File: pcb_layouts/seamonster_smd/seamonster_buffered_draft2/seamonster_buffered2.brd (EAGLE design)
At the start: 172.5 x 106.5 mm, 132 parts, among them IC1 7808DT, IC2 4051D, IC3 4051D, IC4 DG408DY, IC5 4046D, IC6 40106D, IC7 4070D, IC8 4046D, IC9 4040D, Q1 THONKICONNNEW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

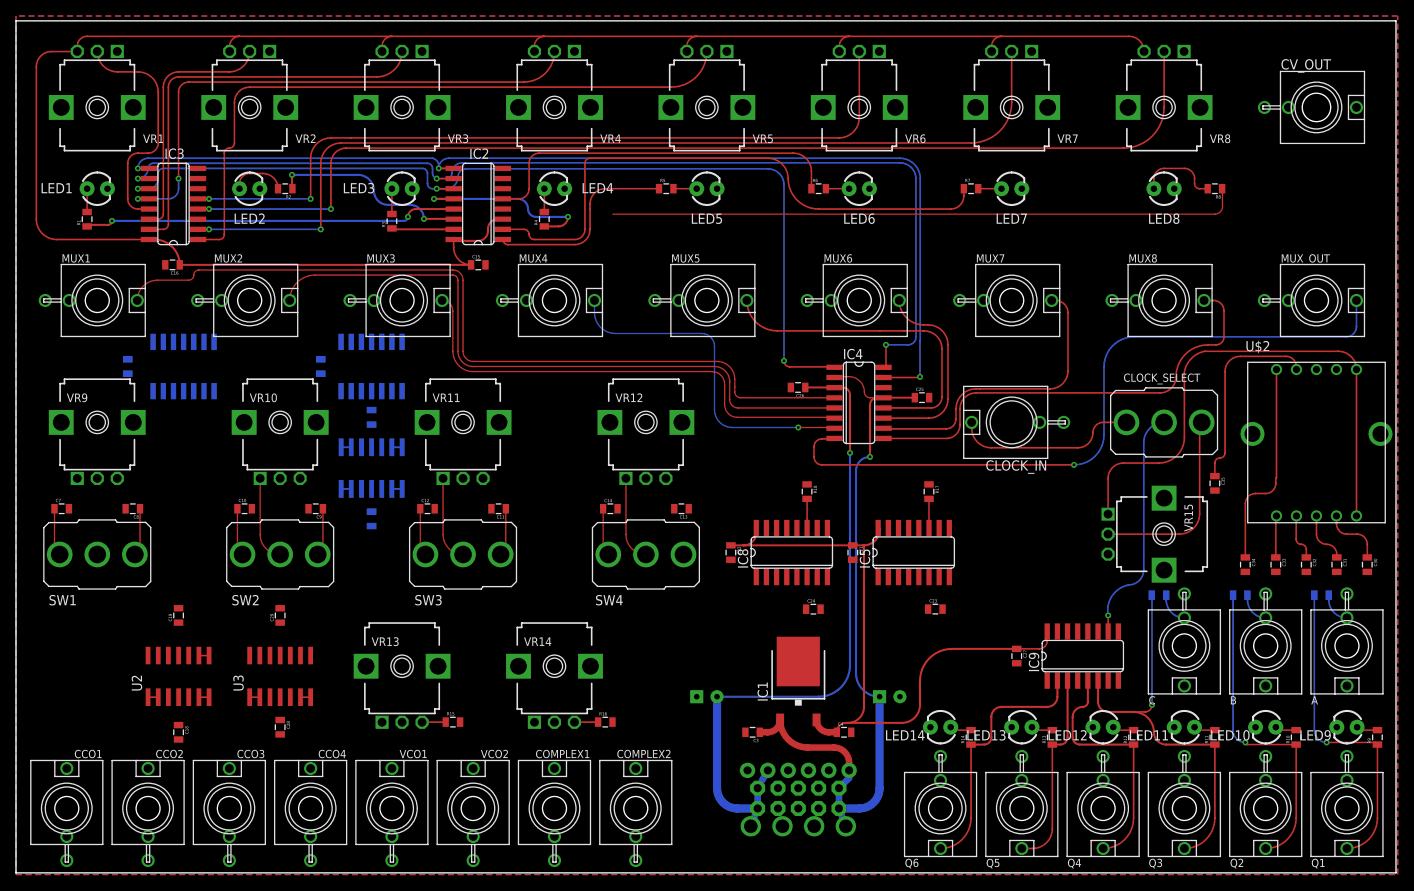
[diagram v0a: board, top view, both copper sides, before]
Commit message: finished routing ABC bus to jacks, began routing oscillators
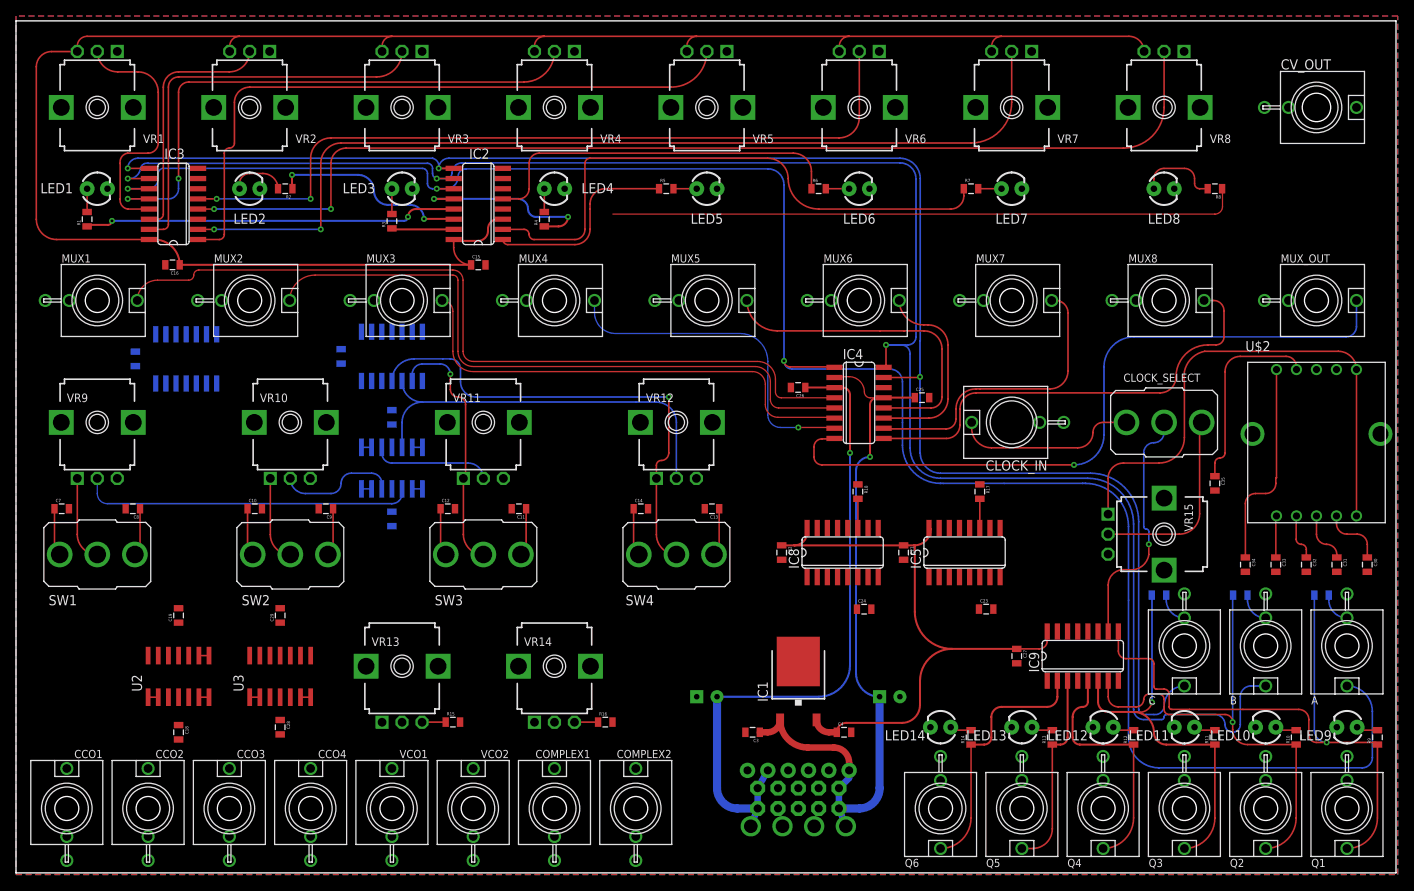
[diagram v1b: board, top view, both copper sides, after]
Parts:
- moved C21 6.35 mm to (111.0, 51.0)
- moved C22 6.35 mm to (95.7, 51.0)
- moved C23 6.35 mm to (121.3, 44.0)
- moved C24 6.35 mm to (106.0, 44.0)
- moved IC5 6.35 mm to (118.6, 51.0)
- moved IC8 6.35 mm to (103.3, 51.0)
- moved R17 6.35 mm to (120.5, 58.7)
- moved R18 6.35 mm to (105.2, 58.7)
- moved C13 3.81 mm to (87.0, 56.5)
- moved C14 3.81 mm to (78.1, 56.5)
- moved SW4 3.81 mm to (82.5, 50.8)
- moved VR12 3.81 mm to (82.5, 67.3)
- moved C17 2.84 mm to (40.6, 75.6)
- moved IC6 2.84 mm to (47.0, 75.6)
- moved C11 2.54 mm to (62.9, 56.5)
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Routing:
- net A: track 118.0 -> 246.0 mm
- net B: track 131.9 -> 227.0 mm
- net C: track 133.2 -> 207.0 mm
- net INV_E_OUT: track 0.00 -> 50.2 mm
- net INV_E_IN: track 10.5 -> 60.0 mm, vias 0 -> 1
- net INV_B_OUT: track 0.00 -> 41.6 mm
- net Q1: track 40.1 -> 77.3 mm
- net Q2: track 40.1 -> 60.7 mm
- net INV_D_IN: track 10.5 -> 31.1 mm, vias 0 -> 1
- net INV_D_OUT: track 0.00 -> 14.7 mm
- net INV_C_OUT: track 0.00 -> 14.5 mm
- net INV_B_IN: track 0.00 -> 10.5 mm
- net VCC: track 325.8 -> 317.6 mm
- net N$64: track 0.00 -> 5.98 mm
- net N$29: track 68.1 -> 70.7 mm
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
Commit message: misc routing for oscillators and buffers
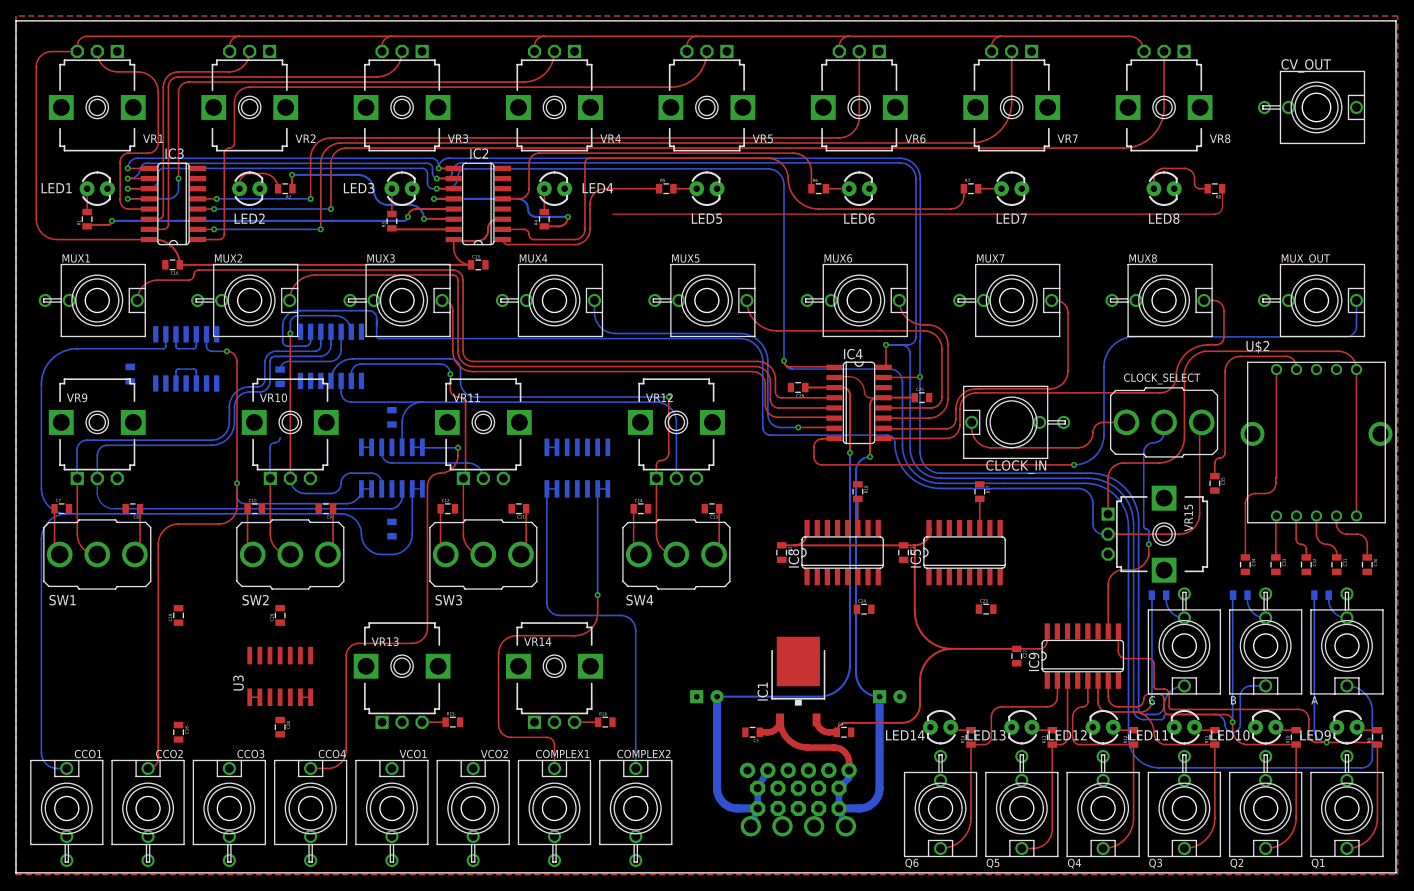
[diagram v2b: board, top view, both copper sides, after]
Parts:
- moved U2 56.2 mm to (70.2, 61.6), flipped to the bottom
- moved C17 8.03 mm to (33.0, 73.0), turned to 270 degrees
- moved IC6 7.62 mm to (39.4, 75.6)
- moved C20 2.01 mm to (14.3, 73.3), turned to 270 degrees
- moved C5 1.27 mm to (47.0, 54.0)
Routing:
- net N$43: track 24.0 -> 154.9 mm
- net CCO1_BUFFERED: track 1.27 -> 124.9 mm
- net CCO2_BUFFERED: track 1.27 -> 84.1 mm, vias 0 -> 2
- net CCO4_BUFFERED: track 1.27 -> 59.2 mm, vias 0 -> 1
- net COMPLEX_OUT1_BUFFERED: track 1.27 -> 51.1 mm, vias 0 -> 1
- net COMPLEX_OUT2_BUFFERED: track 1.27 -> 45.3 mm
- net INV_B_IN: track 10.5 -> 54.0 mm
- net INV_B_OUT: track 41.6 -> 84.4 mm
- net INV_C_OUT: track 14.5 -> 42.7 mm, vias 0 -> 1
- net INV_C_IN: track 10.5 -> 27.0 mm
- net INV_E_OUT: track 50.2 -> 58.7 mm
- net INV_E_IN: track 60.0 -> 67.6 mm
- net INV_D_IN: track 31.1 -> 38.8 mm
- net N$36: track 0.00 -> 5.77 mm
- net N$35: track 0.00 -> 5.77 mm

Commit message: routed bipolar power to buffers, and buffered cv out
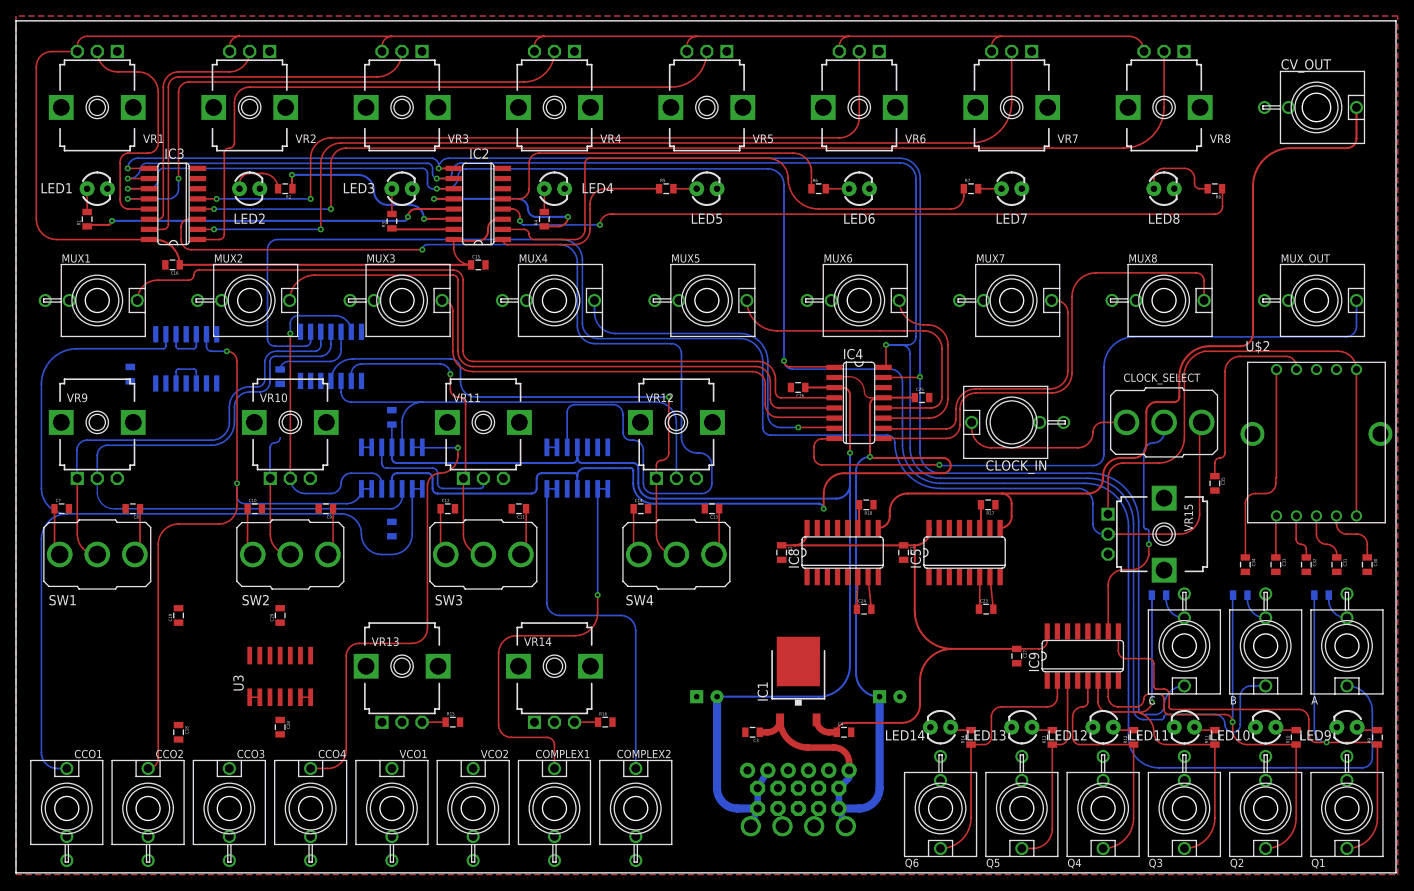
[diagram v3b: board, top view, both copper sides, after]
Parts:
- moved R17 1.96 mm to (121.5, 57.0), turned to 180 degrees
- moved R18 1.96 mm to (106.3, 57.0), turned to 180 degrees
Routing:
- net CV_OUT: track 0.00 -> 127.4 mm, vias 0 -> 1
- net CV_OUT_BUFFERED: track 1.27 -> 105.8 mm
- net V+: track 91.1 -> 185.2 mm, vias 1 -> 2
- net V-: track 83.1 -> 151.5 mm
- net N$43: track 154.9 -> 174.2 mm
- net N$26: track 78.8 -> 94.3 mm, vias 0 -> 2
- net N$44: track 0.00 -> 4.04 mm
- net N$49: track 0.00 -> 4.03 mm
- net N$45: track 0.00 -> 4.02 mm
- net N$48: track 0.00 -> 4.01 mm
- net INV_D_OUT: track 14.7 -> 17.8 mm
- net MUX8: track 55.3 -> 58.2 mm
- net N$1: track 87.9 -> 89.4 mm
- net N$75: track 3.65 -> 2.96 mm
- net N$74: track 3.65 -> 2.96 mm

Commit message: more misc buffer and XOR routing
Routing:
- net CCO3_BUFFERED: track 1.27 -> 94.4 mm, vias 0 -> 2
- net INV_C_IN: track 27.0 -> 35.3 mm
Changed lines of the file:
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@@
 <wire x1="65.0875" y1="60.325" x2="65.7225" y2="60.96" width="0.254" layer="16" curve="-90"/>
 <wire x1="69.85" y1="60.96" x2="70.1675" y2="60.6425" width="0.254" layer="16" curve="-90"/>
-<wire x1="70.1675" y1="60.6425" x2="70.1675" y2="58.995" width="0.254" layer="16"/>
+<wire x1="70.1675" y1="58.995" x2="70.1675" y2="60.6425" width="0.254" layer="16"/>
 <wire x1="47.625" y1="60.96" x2="51.435" y2="60.96" width="0.254" layer="16"/>
 <wire x1="52.07" y1="60.325" x2="52.07" y2="59.055" width="0.254" layer="16"/>
@@
 <contactref element="C32" pad="2"/>
 <contactref element="C31" pad="2"/>
+<wire x1="33.02" y1="72.125" x2="38.79" y2="67.31" width="0" layer="19" extent="16-16"/>
+<wire x1="107.185" y1="57.0075" x2="110.95" y2="50.14" width="0" layer="19" extent="1-1"/>
 <wire x1="46.99" y1="53.075" x2="54.875" y2="56.515" width="0" layer="19" extent="1-16"/>
+<wire x1="122.425" y1="57.0075" x2="123.015" y2="47.9666" width="0" layer="19" extent="1-1"/>
 </signal>
 <signal name="VCC">
@@
 <wire x1="31.79" y1="53.3" x2="34.29" y2="50.8" width="0.2032" layer="1" curve="90"/>
 <wire x1="31.79" y1="60.31" x2="31.75" y2="60.35" width="0.2032" layer="16" curve="-90"/>
-<wire x1="31.75" y1="64.135" x2="32.385" y2="64.77" width="0.2032" layer="16" curve="-90"/>
-<wire x1="32.385" y1="64.77" x2="33.02" y2="65.405" width="0.2032" layer="16" curve="90"/>
-<wire x1="33.02" y1="73.9775" x2="34.29" y2="74.93" width="0.2032" layer="16" curve="-90"/>
-<wire x1="39.37" y1="74.93" x2="40.64" y2="76.5175" width="0.2032" layer="16" curve="90"/>
+<wire x1="40.64" y1="76.5175" x2="39.37" y2="74.93" width="0.2032" layer="16" curve="-90"/>
 <wire x1="40.64" y1="76.5175" x2="40.64" y2="78.6384" width="0.2032" layer="16"/>
-<wire x1="31.75" y1="60.35" x2="31.75" y2="64.135" width="0.2032" layer="16"/>
-<wire x1="34.29" y1="74.93" x2="39.37" y2="74.93" width="0.2032" layer="16"/>
-<wire x1="33.02" y1="65.405" x2="33.02" y2="73.9775" width="0" layer="19" extent="16-16"/>
+<wire x1="39.37" y1="74.93" x2="35.56" y2="74.93" width="0.2032" layer="16"/>
+<wire x1="35.56" y1="74.93" x2="34.29" y2="73.66" width="0.2032" layer="16" curve="90"/>
+<wire x1="34.29" y1="71.12" x2="33.655" y2="70.485" width="0.2032" layer="16" curve="-90"/>
+<wire x1="33.655" y1="70.485" x2="32.7025" y2="70.485" width="0.2032" layer="16"/>
+<wire x1="32.7025" y1="70.485" x2="31.75" y2="69.5325" width="0.2032" layer="16" curve="90"/>
+<wire x1="31.75" y1="69.5325" x2="31.75" y2="60.35" width="0.2032" layer="16"/>
+<wire x1="34.29" y1="73.66" x2="34.29" y2="71.12" width="0.2032" layer="16"/>
 </signal>
 <signal name="INV_C_OUT">
@@
 <wire x1="44.45" y1="58.995" x2="43.18" y2="58.995" width="0.2" layer="16"/>
 <wire x1="43.18" y1="58.995" x2="41.335" y2="57.15" width="0.2032" layer="16" curve="-90"/>
-<via x="27.6225" y="59.69" extent="1-16" drill="0.35"/>
+<via x="26.9875" y="59.69" extent="1-16" drill="0.35"/>
 <wire x1="23.8125" y1="78.3209" x2="23.8125" y2="76.835" width="0.2032" layer="16"/>
 <wire x1="23.8125" y1="76.835" x2="24.4475" y2="76.2" width="0.2032" layer="16" curve="90"/>
 <wire x1="24.4475" y1="76.2" x2="26.3525" y2="76.2" width="0.2032" layer="16"/>
 <via x="26.3525" y="76.2" extent="1-16" drill="0.35"/>
-<wire x1="26.3525" y1="76.2" x2="27.6225" y2="74.93" width="0.2032" layer="1" curve="-90"/>
-<wire x1="27.6225" y1="74.93" x2="27.6225" y2="59.69" width="0.2032" layer="1"/>
+<wire x1="26.3525" y1="76.2" x2="26.9875" y2="75.565" width="0.2032" layer="1" curve="-90"/>
+<wire x1="26.9875" y1="75.565" x2="26.9875" y2="59.69" width="0.2032" layer="1"/>
 <wire x1="41.335" y1="57.15" x2="28.575" y2="57.15" width="0.2032" layer="16"/>
-<wire x1="28.575" y1="57.15" x2="27.6225" y2="58.1025" width="0.2032" layer="16" curve="-90"/>
-<wire x1="27.6225" y1="58.1025" x2="27.6225" y2="59.69" width="0.2032" layer="16"/>
-<wire x1="27.6225" y1="59.69" x2="27.6225" y2="56.8325" width="0.2032" layer="1"/>
-<wire x1="27.6225" y1="56.8325" x2="25.4" y2="54.61" width="0.2032" layer="1" curve="-90"/>
+<wire x1="28.575" y1="57.15" x2="26.9875" y2="58.1025" width="0.2032" layer="16" curve="-90"/>
+<wire x1="26.9875" y1="58.1025" x2="26.9875" y2="59.69" width="0.2032" layer="16"/>
+<wire x1="26.9875" y1="59.69" x2="26.9875" y2="56.515" width="0.2032" layer="1"/>
+<wire x1="26.9875" y1="56.515" x2="25.4" y2="54.61" width="0.2032" layer="1" curve="-90"/>
 <wire x1="20.32" y1="54.61" x2="17.78" y2="52.07" width="0.2032" layer="1" curve="90"/>
 <wire x1="17.78" y1="25.32" x2="16.51" y2="24.05" width="0.2032" layer="1" curve="-90"/>
@@
 <contactref element="IC7" pad="9"/>
 <contactref element="CCO3" pad="P$1_TIP"/>
-<wire x1="44.45" y1="64.195" x2="43.18" y2="64.195" width="0.2" layer="16"/>
-<wire x1="23.8125" y1="72.1741" x2="43.18" y2="64.195" width="0" layer="19" extent="16-16"/>
-<wire x1="26.67" y1="24.05" x2="43.18" y2="64.195" width="0" layer="19" extent="16-16"/>
+<wire x1="43.18" y1="64.195" x2="44.45" y2="64.195" width="0.2" layer="16"/>
+<wire x1="23.8125" y1="72.1741" x2="23.8125" y2="73.3425" width="0.2032" layer="16"/>
+<wire x1="26.67" y1="24.05" x2="26.59" y2="24.13" width="0.2032" layer="1" curve="90"/>
+<wire x1="26.59" y1="24.13" x2="20.32" y2="24.13" width="0.2032" layer="1"/>
+<wire x1="20.32" y1="24.13" x2="18.415" y2="26.035" width="0.2032" layer="1" curve="-90"/>
+<wire x1="18.415" y1="52.07" x2="20.32" y2="53.975" width="0.2032" layer="1" curve="-90"/>
+<wire x1="18.415" y1="26.035" x2="18.415" y2="52.07" width="0.2032" layer="1"/>
+<wire x1="20.32" y1="53.975" x2="25.4" y2="53.975" width="0.2032" layer="1"/>
+<wire x1="25.4" y1="53.975" x2="27.94" y2="56.515" width="0.2032" layer="1" curve="90"/>
+<wire x1="27.94" y1="73.66" x2="27.94" y2="74.295" width="0.2032" layer="1"/>
+<wire x1="27.94" y1="73.66" x2="27.94" y2="74.295" width="0.2032" layer="1"/>
+<via x="27.94" y="74.295" extent="1-16" drill="0.35"/>
+<wire x1="23.8125" y1="73.3425" x2="24.765" y2="74.295" width="0.2032" layer="16" curve="-90"/>
+<wire x1="24.765" y1="74.295" x2="27.94" y2="74.295" width="0.2032" layer="16"/>
+<wire x1="27.94" y1="56.515" x2="27.94" y2="63.5" width="0.2032" layer="1"/>
+<wire x1="27.94" y1="63.5" x2="27.94" y2="73.66" width="0.2032" layer="1"/>
+<wire x1="27.94" y1="63.5" x2="29.21" y2="62.23" width="0.2032" layer="1" curve="90"/>
+<wire x1="29.21" y1="62.23" x2="31.75" y2="62.23" width="0.2032" layer="1"/>
+<wire x1="31.75" y1="62.23" x2="33.02" y2="60.96" width="0.2032" layer="1" curve="-90"/>
+<wire x1="33.02" y1="60.96" x2="33.02" y2="59.69" width="0.2032" layer="1"/>
+<wire x1="33.02" y1="59.69" x2="34.29" y2="58.42" width="0.2032" layer="1" curve="90"/>
+<wire x1="39.37" y1="58.42" x2="40.64" y2="59.69" width="0.2032" layer="1" curve="90"/>
+<wire x1="40.64" y1="63.1825" x2="41.5925" y2="64.135" width="0.2032" layer="1" curve="-90"/>
+<via x="41.5925" y="64.135" extent="1-16" drill="0.35"/>
+<wire x1="41.5925" y1="64.135" x2="43.12" y2="64.135" width="0.2032" layer="16"/>
+<wire x1="43.12" y1="64.135" x2="43.18" y2="64.195" width="0.2032" layer="16" curve="90"/>
+<wire x1="34.29" y1="58.42" x2="39.37" y2="58.42" width="0.2032" layer="1"/>
+<wire x1="40.64" y1="59.69" x2="40.64" y2="63.1825" width="0.2032" layer="1"/>
 </signal>
 <signal name="CCO4_BUFFERED">
